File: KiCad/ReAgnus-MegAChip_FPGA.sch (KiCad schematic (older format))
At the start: 2 parts, among them U5 GW1N-UV9LQ144

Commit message: more routing and placing components
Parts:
- renumbered U5 to U7
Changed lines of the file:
@@
 AR Path="/632F85D3" Ref="U?"  Part="1"
 AR Path="/632D3BDF/632F85D3" Ref="U?"  Part="1"
-AR Path="/632F104D/632F85D3" Ref="U5"  Part="1"
-F 0 "U5" H 3400 3450 60  0000 R CNN
+AR Path="/632F104D/632F85D3" Ref="U7"  Part="1"
+F 0 "U7" H 3400 3450 60  0000 R CNN
 F 1 "GW1N-UV9LQ144" H 3750 3600 60  0000 R CNN
 F 2 "Package_QFP:EQFP-144-1EP_20x20mm_P0.5mm_EP5x5mm" H 3350 3700 60  0001 C CNN

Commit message: more routing and placing components
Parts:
- U7: footprint Package_QFP:EQFP-144-1EP_20x20mm_P0.5mm_EP5x5mm -> Package_QFP:LQFP-144_20x20mm_P0.5mm
- renumbered C2 to C9
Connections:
- net labels added: A10_3V3, A11_3V3, A12_3V3, A13_3V3, A14_3V3, A15_3V3, A16_3V3, A17_3V3, A18_3V3, A19_3V3, A1_3V3, A2_3V3, A3_3V3, A4_3V3, A5_3V3, A6_3V3, A7_3V3, A8_3V3, A9_3V3, CASL|UDS_3V3, CASU|CASL_3V3, CSYNC_3V3, DRA0_3V3|GND, DRA1|DRA0_3V3, DRA2|DRA1_3V3, DRA3|DRA2_3V3, DRA4|DRA3_3V3, DRA5|DRA4_3V3, DRA6|DRA5_3V3, DRA7|DRA6_3V3, DRA8|DRA7_3V3, DRA8|LDS_3V3, DRA9|CASU_3V3, HSYNC_3V3, LDS|UDS_3V3, LPEN_3V3, RAS0|RAS_3V3, RAS1|DRA9_3V3, VSYNC_3V3, XLCK|A20_3V3
- net labels removed: A12
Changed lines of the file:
@@
 Comment4 ""
 $EndDescr
-Text GLabel 3900 6350 3    50   Input ~ 0
+Text GLabel 7000 4300 0    50   Input ~ 0
 GND
 Text GLabel 7300 5200 2    50   Input ~ 0
@@
 AR Path="/632F85C6" Ref="C?"  Part="1"
 AR Path="/632D3BDF/632F85C6" Ref="C?"  Part="1"
-AR Path="/632F104D/632F85C6" Ref="C2"  Part="1"
-F 0 "C2" H 7142 5100 50  0000 L CNN
+AR Path="/632F104D/632F85C6" Ref="C9"  Part="1"
+F 0 "C9" H 7142 5100 50  0000 L CNN
 F 1 "C_Small" H 7142 5055 50  0001 L CNN
 F 2 "Capacitor_SMD:C_1206_3216Metric_Pad1.42x1.75mm_HandSolder" H 7050 5100 50  0001 C CNN
@@
 F 0 "U7" H 3400 3450 60  0000 R CNN
 F 1 "GW1N-UV9LQ144" H 3750 3600 60  0000 R CNN
-F 2 "Package_QFP:EQFP-144-1EP_20x20mm_P0.5mm_EP5x5mm" H 3350 3700 60  0001 C CNN
+F 2 "Package_QFP:LQFP-144_20x20mm_P0.5mm" H 3350 3700 60  0001 C CNN
 F 3 "https://www.mouser.com/datasheet/2/1033/GW1N_series_of_FPGA_Products_Data_Sheet-1830682.pdf" H 4800 4800 60  0001 C CNN
 	1    3350 3600
@@
 A13
 Text GLabel 8600 2150 0    50   Input ~ 0
-A12
+A12_3V3
 Text GLabel 8600 2250 0    50   Input ~ 0
 A11
@@
 Text GLabel 10400 4900 2    50   Input ~ 0
 GND|NTSC
+Text GLabel 5800 5350 2    50   Input ~ 0
+A18_3V3
+Text GLabel 5800 5450 2    50   Input ~ 0
+A19_3V3
+Text GLabel 5800 5250 2    50   Input ~ 0
+A17_3V3
+Text GLabel 5800 5050 2    50   Input ~ 0
+A16_3V3
+Text GLabel 5800 4950 2    50   Input ~ 0
+A15_3V3
+Text GLabel 5800 4850 2    50   Input ~ 0
+A14_3V3
+Text GLabel 5800 4750 2    50   Input ~ 0
+A13_3V3
+Text GLabel 5800 3850 2    50   Input ~ 0
+A12_3V3
+Text GLabel 5800 3950 2    50   Input ~ 0
+A11_3V3
+Text GLabel 5800 4050 2    50   Input ~ 0
+A10_3V3
+Text GLabel 5800 4150 2    50   Input ~ 0
+A9_3V3
+Text GLabel 5800 4250 2    50   Input ~ 0
+A8_3V3
+Text GLabel 5800 4350 2    50   Input ~ 0
+A7_3V3
+Text GLabel 5800 4450 2    50   Input ~ 0
+A6_3V3
+Text GLabel 5800 4600 2    50   Input ~ 0
+A5_3V3
+Text GLabel 5800 5150 2    50   Input ~ 0
+XLCK|A20_3V3
+Text GLabel 4900 6050 3    50   BiDi ~ 0
+HSYNC_3V3
+Text GLabel 5000 6050 3    50   Output ~ 0
+CSYNC_3V3
+Text GLabel 5800 5650 2    50   BiDi ~ 0
+VSYNC_3V3
+Text GLabel 5800 5550 2    50   Input ~ 0
+LPEN_3V3
+Text GLabel 5800 3750 2    50   Input ~ 0
+A4_3V3
+Text GLabel 5800 3650 2    50   Input ~ 0
+A3_3V3
+Text GLabel 5800 3550 2    50   Input ~ 0
+A2_3V3
+Text GLabel 5800 3450 2    50   Input ~ 0
+A1_3V3
+Text GLabel 5800 3150 2    50   Output ~ 0
+RAS0|RAS_3V3
+Text GLabel 5800 3300 2    50   Output ~ 0
+RAS1|DRA9_3V3
+Text GLabel 6700 1750 2    50   Input ~ 0
+DRA9|CASU_3V3
+Text GLabel 6700 1850 2    50   Input ~ 0
+CASU|CASL_3V3
+Text GLabel 6700 1950 2    50   Input ~ 0
+CASL|UDS_3V3
+Text GLabel 6700 2150 2    50   Output ~ 0
+LDS|UDS_3V3
+Text GLabel 6700 2250 2    50   Output ~ 0
+DRA8|LDS_3V3
+Text GLabel 6700 2350 2    50   Input ~ 0
+DRA8|DRA7_3V3
+Text GLabel 6700 2850 2    50   Input ~ 0
+DRA7|DRA6_3V3
+Text GLabel 6700 3050 2    50   Input ~ 0
+DRA6|DRA5_3V3
+Text GLabel 6700 3150 2    50   Input ~ 0
+DRA5|DRA4_3V3
+Text GLabel 6700 3250 2    50   Input ~ 0
+DRA4|DRA3_3V3
+Text GLabel 6700 3350 2    50   Input ~ 0
+DRA3|DRA2_3V3
+Text GLabel 6700 3450 2    50   Input ~ 0
+DRA2|DRA1_3V3
+Text GLabel 6700 3550 2    50   Input ~ 0
+DRA1|DRA0_3V3
+Text GLabel 6700 3650 2    50   Input ~ 0
+DRA0_3V3|GND
 $EndSCHEMATC

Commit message: more routing and placing components
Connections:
- net labels added: 14M|CCK_3V3, 28M_3V3, 7M|CDAC_3V3, AS_3V3, BLIT_3V3, CCKQ|7M_3V3, CCK|CCKQ_3V3, CDAC|XCLKEN_3V3, RAMEN_3V3, REGEN_3V3, RGA1_3V3, RGA2_3V3, RGA3_3V3, RGA4_3V3, RGA5_3V3, RGA6_3V3, RGA7_3V3, RGA8_3V3, RW_3V3, WE_3V3
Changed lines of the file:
@@
 Text GLabel 6700 3650 2    50   Input ~ 0
 DRA0_3V3|GND
+Text GLabel -500 4050 2    50   Input ~ 0
+BLIT_3V3
+Text GLabel -500 3950 2    50   Input ~ 0
+WE_3V3
+Text GLabel -500 3850 2    50   Output ~ 0
+RW_3V3
+Text GLabel -500 3750 2    50   Output ~ 0
+REGEN_3V3
+Text GLabel -500 3650 2    50   Output ~ 0
+AS_3V3
+Text GLabel 900  3300 0    50   Input ~ 0
+RAMEN_3V3
+Text GLabel 900  3200 0    50   Input ~ 0
+28M_3V3
+Text GLabel 7400 1950 2    50   Input ~ 0
+CCKQ|7M_3V3
+Text GLabel 7400 1850 2    50   Input ~ 0
+CCK|CCKQ_3V3
+Text GLabel 7400 1750 2    50   Input ~ 0
+14M|CCK_3V3
+Text GLabel 7400 2050 2    50   Input ~ 0
+7M|CDAC_3V3
+Text GLabel 7400 2150 2    50   BiDi ~ 0
+CDAC|XCLKEN_3V3
+Text GLabel 900  5000 0    50   Output ~ 0
+RGA1_3V3
+Text GLabel 900  4900 0    50   Output ~ 0
+RGA2_3V3
+Text GLabel 900  4800 0    50   Output ~ 0
+RGA3_3V3
+Text GLabel 900  4700 0    50   Output ~ 0
+RGA4_3V3
+Text GLabel 900  4600 0    50   Output ~ 0
+RGA5_3V3
+Text GLabel 900  4500 0    50   Output ~ 0
+RGA6_3V3
+Text GLabel 900  4400 0    50   Output ~ 0
+RGA7_3V3
+Text GLabel 900  3600 0    50   Output ~ 0
+RGA8_3V3
 $EndSCHEMATC

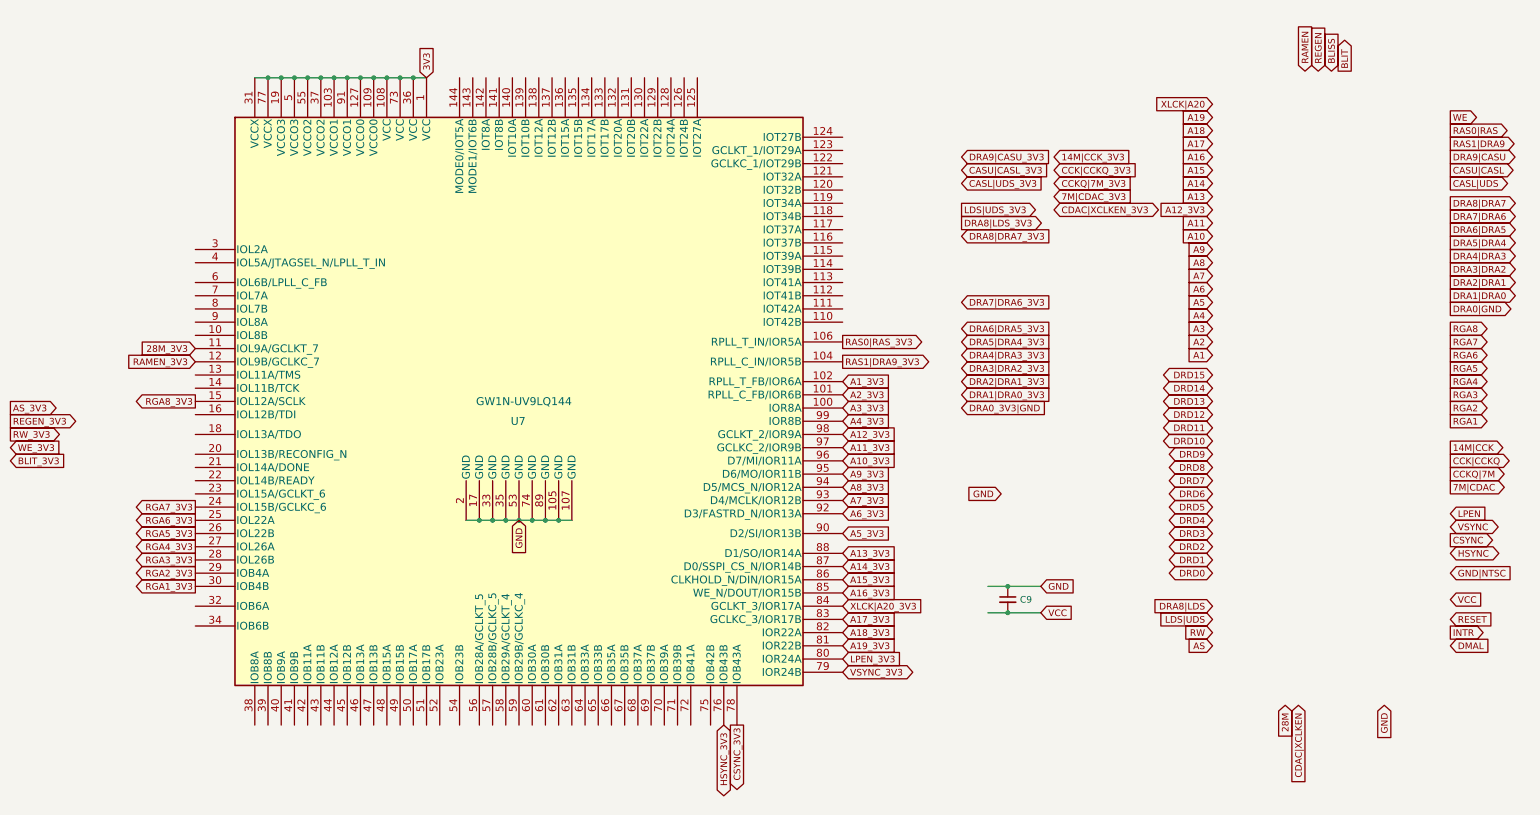
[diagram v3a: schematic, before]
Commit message: major redesign of PCB done
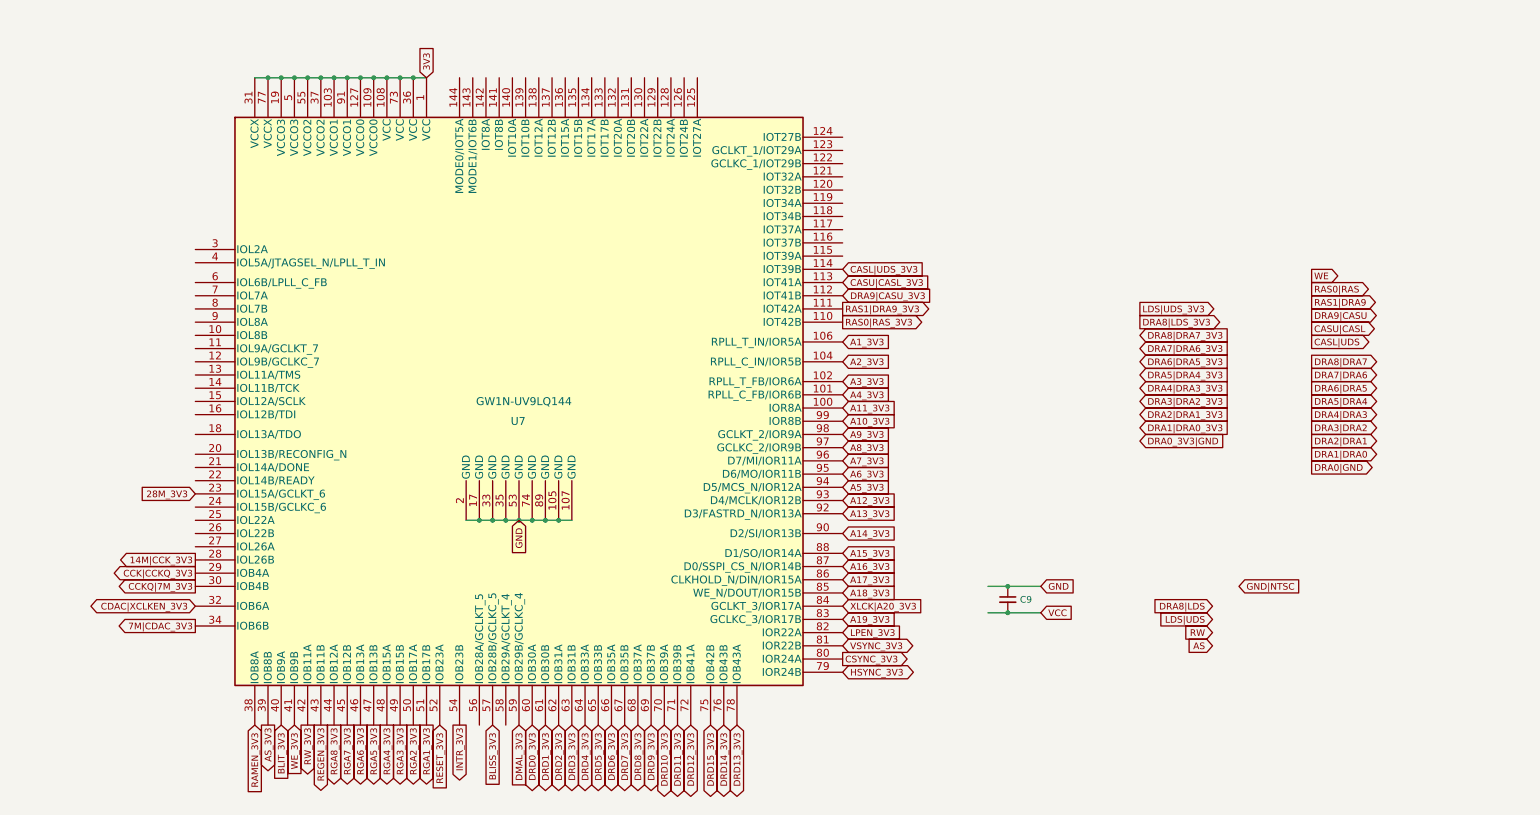
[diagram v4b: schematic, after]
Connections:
- net labels added: BLISS_3V3, DMAL_3V3, DRD0_3V3, DRD10_3V3, DRD11_3V3, DRD12_3V3, DRD13_3V3, DRD14_3V3, DRD15_3V3, DRD1_3V3, DRD2_3V3, DRD3_3V3, DRD4_3V3, DRD5_3V3, DRD6_3V3, DRD7_3V3, DRD8_3V3, DRD9_3V3, INTR_3V3, RESET_3V3
- net labels removed: 14M|CCK, 28M, 7M|CDAC, A1, A10, A11, A13, A14, A15, A16, A17, A18, A19, A2, A3, A4, A5, A6, A7, A8, A9, BLISS, BLIT, CCKQ|7M, CCK|CCKQ, CDAC|XCLKEN, CSYNC, DMAL, DRD0, DRD1, DRD10, DRD11, DRD12, DRD13, DRD14, DRD15, DRD2, DRD3, DRD4, DRD5, DRD6, DRD7, DRD8, DRD9, HSYNC, INTR, LPEN, RAMEN, REGEN, RESET, RGA1, RGA2, RGA3, RGA4, RGA5, RGA6, RGA7, RGA8, VSYNC, XLCK|A20

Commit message: added 74LVC1G07 buffer with open-drain output
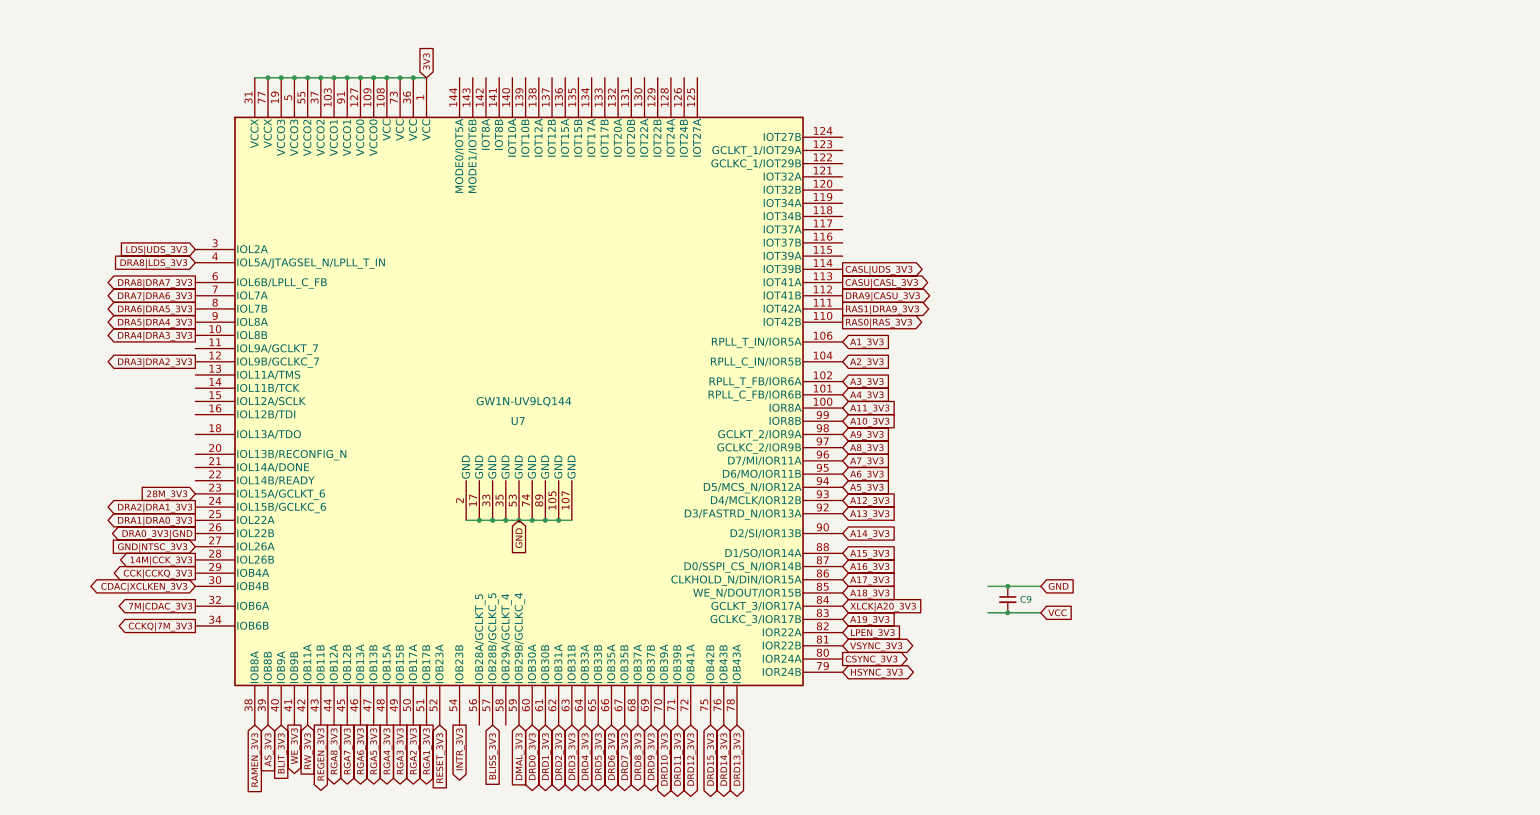
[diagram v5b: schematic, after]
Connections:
- net labels added: GND|NTSC_3V3
- net labels removed: AS, CASL|UDS, CASU|CASL, DRA0|GND, DRA1|DRA0, DRA2|DRA1, DRA3|DRA2, DRA4|DRA3, DRA5|DRA4, DRA6|DRA5, DRA7|DRA6, DRA8|DRA7, DRA8|LDS, DRA9|CASU, GND|NTSC, LDS|UDS, RAS0|RAS, RAS1|DRA9, RW, WE
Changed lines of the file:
@@
 Wire Wire Line
 	2550 1150 2450 1150
-Text GLabel 9350 4100 2    50   Output ~ 0
-DRA0|GND
-Text GLabel 9350 4000 2    50   Output ~ 0
-DRA1|DRA0
-Text GLabel 9350 3900 2    50   Output ~ 0
-DRA2|DRA1
-Text GLabel 9350 3800 2    50   Output ~ 0
-DRA3|DRA2
-Text GLabel 9350 3700 2    50   Output ~ 0
-DRA4|DRA3
-Text GLabel 9350 3600 2    50   Output ~ 0
-DRA5|DRA4
-Text GLabel 9350 3500 2    50   Output ~ 0
-DRA6|DRA5
-Text GLabel 9350 3400 2    50   Output ~ 0
-DRA7|DRA6
-Text GLabel 9350 3300 2    50   Output ~ 0
-DRA8|DRA7
-Text GLabel 9350 2850 2    50   Output ~ 0
-RAS1|DRA9
-Text GLabel 9350 2750 2    50   Output ~ 0
-RAS0|RAS
-Text GLabel 9350 3050 2    50   Output ~ 0
-CASU|CASL
-Text GLabel 9350 2650 2    50   Output ~ 0
-WE
-Text GLabel 8600 5450 0    50   Input ~ 0
-AS
-Text GLabel 8600 5350 0    50   Input ~ 0
-RW
 Text GLabel 3450 6050 3    50   BiDi ~ 0
 DRD0_3V3
@@
 Text GLabel 4800 6050 3    50   BiDi ~ 0
 DRD15_3V3
-Text GLabel 8600 5150 0    50   Input ~ 0
-DRA8|LDS
-Text GLabel 8600 5250 0    50   Input ~ 0
-LDS|UDS
-Text GLabel 9350 3150 2    50   Output ~ 0
-CASL|UDS
-Text GLabel 9350 2950 2    50   Output ~ 0
-DRA9|CASU
-Text GLabel 8800 5000 2    50   Input ~ 0
-GND|NTSC
+Text GLabel 900  4700 0    50   Input ~ 0
+GND|NTSC_3V3
 Text GLabel 5800 5050 2    50   Input ~ 0
 A18_3V3
@@
 Text GLabel 5800 2900 2    50   Output ~ 0
 RAS1|DRA9_3V3
-Text GLabel 5800 2800 2    50   Input ~ 0
+Text GLabel 5800 2800 2    50   Output ~ 0
 DRA9|CASU_3V3
-Text GLabel 5800 2700 2    50   Input ~ 0
+Text GLabel 5800 2700 2    50   Output ~ 0
 CASU|CASL_3V3
-Text GLabel 5800 2600 2    50   Input ~ 0
+Text GLabel 5800 2600 2    50   Output ~ 0
 CASL|UDS_3V3
-Text GLabel 8050 2900 2    50   Output ~ 0
+Text GLabel 900  2450 0    50   Input ~ 0
 LDS|UDS_3V3
-Text GLabel 8050 3000 2    50   Output ~ 0
+Text GLabel 900  2550 0    50   Input ~ 0
 DRA8|LDS_3V3
-Text GLabel 8050 3100 2    50   Input ~ 0
+Text GLabel 900  2700 0    50   Output ~ 0
 DRA8|DRA7_3V3
-Text GLabel 8050 3200 2    50   Input ~ 0
+Text GLabel 900  2800 0    50   Output ~ 0
 DRA7|DRA6_3V3
-Text GLabel 8050 3300 2    50   Input ~ 0
+Text GLabel 900  2900 0    50   Output ~ 0
 DRA6|DRA5_3V3
-Text GLabel 8050 3400 2    50   Input ~ 0
+Text GLabel 900  3000 0    50   Output ~ 0
 DRA5|DRA4_3V3
-Text GLabel 8050 3500 2    50   Input ~ 0
+Text GLabel 900  3100 0    50   Output ~ 0
 DRA4|DRA3_3V3
-Text GLabel 8050 3600 2    50   Input ~ 0
+Text GLabel 900  3300 0    50   Output ~ 0
 DRA3|DRA2_3V3
-Text GLabel 8050 3700 2    50   Input ~ 0
+Text GLabel 900  4400 0    50   Output ~ 0
 DRA2|DRA1_3V3
-Text GLabel 8050 3800 2    50   Input ~ 0
+Text GLabel 900  4500 0    50   Output ~ 0
 DRA1|DRA0_3V3
-Text GLabel 8050 3900 2    50   Input ~ 0
+Text GLabel 900  4600 0    50   Output ~ 0
 DRA0_3V3|GND
 Text GLabel 1550 6050 3    50   Input ~ 0
 BLIT_3V3
-Text GLabel 1650 6050 3    50   Input ~ 0
+Text GLabel 1650 6050 3    50   Output ~ 0
 WE_3V3
-Text GLabel 1750 6050 3    50   Output ~ 0
+Text GLabel 1750 6050 3    50   Input ~ 0
 RW_3V3
 Text GLabel 1850 6050 3    50   Output ~ 0
 REGEN_3V3
-Text GLabel 1450 6050 3    50   Output ~ 0
+Text GLabel 1450 6050 3    50   Input ~ 0
 AS_3V3
 Text GLabel 1350 6050 3    50   Input ~ 0
@@
 Text GLabel 900  4300 0    50   Input ~ 0
 28M_3V3
-Text GLabel 900  5000 0    50   Output ~ 0
+Text GLabel 900  5300 0    50   Output ~ 0
 CCKQ|7M_3V3
 Text GLabel 900  4900 0    50   Output ~ 0
@@
 Text GLabel 900  4800 0    50   Output ~ 0
 14M|CCK_3V3
-Text GLabel 900  5300 0    50   Output ~ 0
+Text GLabel 900  5150 0    50   Output ~ 0
 7M|CDAC_3V3
-Text GLabel 900  5150 0    50   BiDi ~ 0
+Text GLabel 900  5000 0    50   BiDi ~ 0
 CDAC|XCLKEN_3V3
 Text GLabel 2650 6050 3    50   Output ~ 0

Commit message: more routing
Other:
- moved on the sheet: C9, U7
